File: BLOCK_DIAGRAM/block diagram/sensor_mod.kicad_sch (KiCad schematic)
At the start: 2 parts, among them U12 MQ-6, U7 LM393

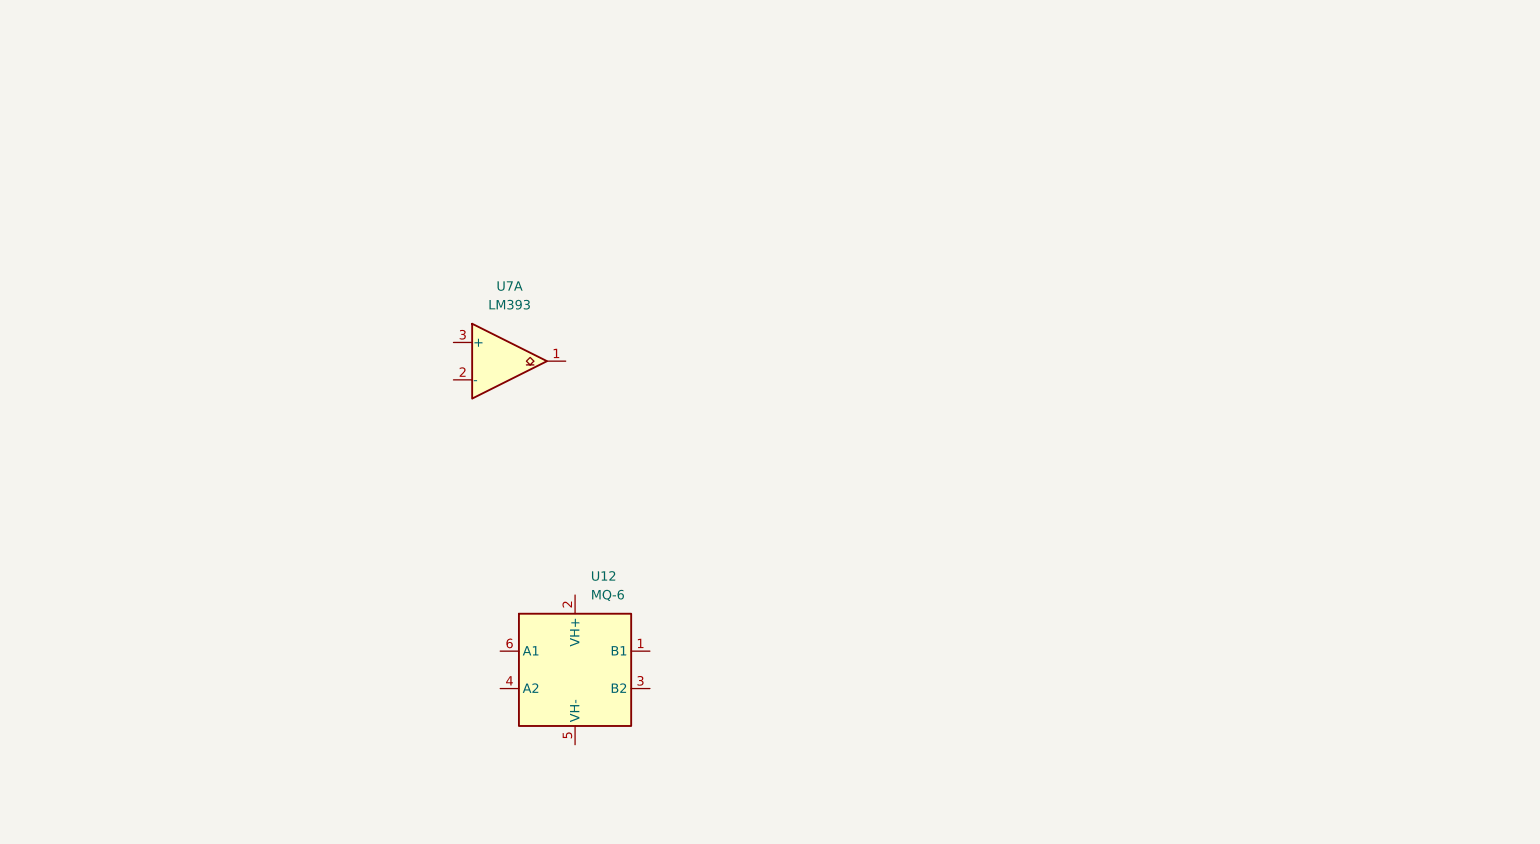
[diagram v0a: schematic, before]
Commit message: edited the connections of the 220-5 (added the RLC) and added RLC for en pullup and 3v3 of esp
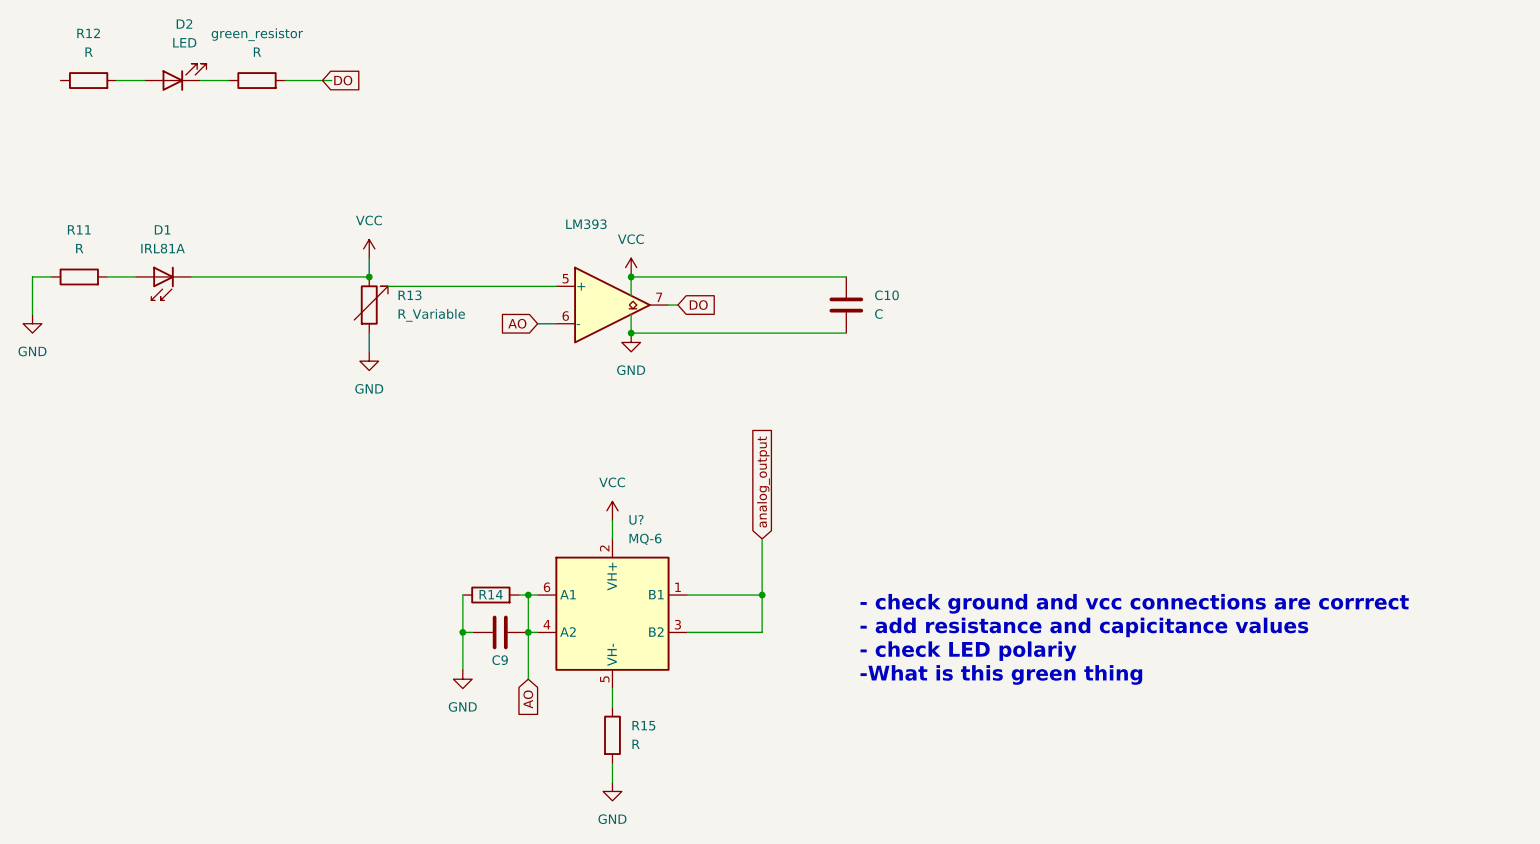
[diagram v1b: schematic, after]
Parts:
- removed U7: LM393, symbol Comparator:LM393
- added C10, C9: C, symbol Device:C
- added D1: IRL81A, LED_THT:LED_SideEmitter_Rectangular_W4.5mm_H1.6mm, symbol LED:IRL81A
- added D2: LED, symbol Device:LED
- added R11, R12, R14, R15, green_resistor: R, symbol Device:R
- added R13: R_Variable, symbol Device:R_Variable
- added U7: LM393, symbol Comparator:LM393
- renumbered U12 to U?
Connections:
- net analog_output: now reaches U?.1 (B1)
- net analog_output: now also U?.3 (B2)
- net VCC: now reaches U?.2 (VH+)
- net VCC: now also C10.1, D1.1 (K), R13.1
- net AO: now reaches U?.4 (A2)
- net AO: now also U?.6 (A1), C9.1, R14.2, U7.6 (-)
- net at U?.5 (VH-): now also R15.1
- new net: D2.2 (A), R12.2
- new net: D2.1 (K), green_resistor.1
- new net: D1.2 (A), R11.2
- new net DO: U7.7, green_resistor.2
- new net GND: C10.2, C9.2, R11.1, R13.2, R14.1, R15.2
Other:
- note added: "- check ground and vcc connections are corrrect - add resistance and capicitance values - check LED polariy -What is this green thing"
- moved on the sheet: U?
